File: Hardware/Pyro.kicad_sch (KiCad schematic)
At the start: 10 parts, among them J5 7788, J6 7788, Q1 BUK9M11-40EX, U12 TCMT1109

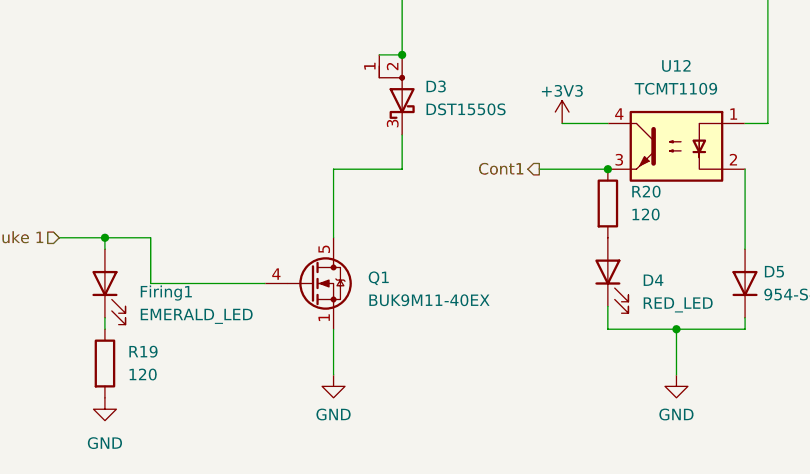
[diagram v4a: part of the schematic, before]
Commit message: GPIO broken out + post review 4
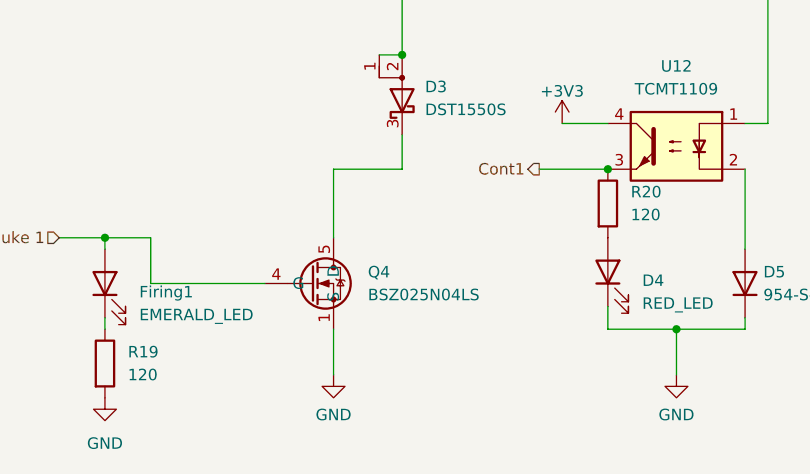
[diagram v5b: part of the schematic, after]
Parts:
- removed Q1: BUK9M11-40EX, Package_TO_SOT_SMD:LFPAK33, symbol Transistor_FET:BUK9M11-40EX
- added Q4: BSZ025N04LS, iclr:BSZ025N04LS, symbol iclr:BSZ025N04LS
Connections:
- net GND: now also Q4.1 (S), Q4.2 (S), Q4.3 (S), Q4.A1 (S)
- net Nuke 1: now also Q4.4 (G)
- net at D3.3 (K): now also Q4.5 (D), Q4.6 (D), Q4.7 (D), Q4.8 (D), Q4.A5 (D)
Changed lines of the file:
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@@
+	)
+	(symbol
+		(lib_id "iclr:BSZ025N04LS")
+		(at 114.3 95.25 0)
+		(unit 1)
+		(exclude_from_sim no)
+		(in_bom yes)
+		(on_board yes)
+		(dnp no)
+		(fields_autoplaced yes)
+		(property "Reference" "Q4"
+			(at 119.38 93.9799 0)
+			(effects
+				(font
+					(size 1.27 1.27)
+				)
+				(justify left)
+			)
+		)
+		(property "Value" "BSZ025N04LS"
+			(at 119.38 96.5199 0)
+			(effects
+				(font
+					(size 1.27 1.27)
+				)
+				(justify left)
+			)
+		)
+		(property "Footprint" "iclr:BSZ025N04LS"
+			(at 135.89 190.17 0)
+			(effects
+				(font
+					(size 1.27 1.27)
+				)
+				(justify left top)
+				(hide yes)
+			)
+		)
+		(property "Datasheet" "http://www.infineon.com/dgdl/DS_BSZ025N04LS_2_1.pdf?fileId=5546d46146d18cb40147204a34530283"
+			(at 135.89 290.17 0)
+			(effects
+				(font
+					(size 1.27 1.27)
+				)
+				(justify left top)
+				(hide yes)
+			)
+		)
+		(property "Description" "MOSFET MV POWER MOS MOSFET OptiMOS Power-MOSFET,40V"
+			(at 114.554 74.168 0)
+			(effects
+				(font
+					(size 1.27 1.27)
+				)
+				(hide yes)
+			)
+		)
+		(property "Height" "1.1"
+			(at 135.89 490.17 0)
+			(effects
+				(font
+					(size 1.27 1.27)
+				)
+				(justify left top)
+				(hide yes)
+			)
+		)
+		(property "Manufacturer_Name" "Infineon"
+			(at 135.89 590.17 0)
+			(effects
+				(font
+					(size 1.27 1.27)
+				)
+				(justify left top)
+				(hide yes)
+			)
+		)
+		(property "Manufacturer_Part_Number" "BSZ025N04LS"
+			(at 135.89 690.17 0)
+			(effects
+				(font
+					(size 1.27 1.27)
+				)
+				(justify left top)
+				(hide yes)
+			)
+		)
+		(property "Mouser Part Number" "726-BSZ025N04LS"
+			(at 135.89 790.17 0)
+			(effects
+				(font
+					(size 1.27 1.27)
+				)
+				(justify left top)
+				(hide yes)
+			)
+		)
+		(property "Mouser Price/Stock" "https://www.mouser.co.uk/ProductDetail/Infineon-Technologies/BSZ025N04LS?qs=glduVv6OWv6ppMJu86R39g%3D%3D"
+			(at 135.89 890.17 0)
+			(effects
+				(font
+					(size 1.27 1.27)
+				)
+				(justify left top)
+				(hide yes)
+			)
+		)
+		(property "Arrow Part Number" ""
+			(at 135.89 990.17 0)
+			(effects
+				(font
+					(size 1.27 1.27)
+				)
+				(justify left top)
+				(hide yes)
+			)
+		)
+		(property "Arrow Price/Stock" ""
+			(at 135.89 1090.17 0)
+			(effects
+				(font
+					(size 1.27 1.27)
+				)
+				(justify left top)
+				(hide yes)
+			)
+		)
+		(pin "6"
+		)
+		(pin "1"
+		)
+		(pin "A1"
+		)
+		(pin "A5"
+		)
+		(pin "7"
+		)
+		(pin "4"
+		)
+		(pin "5"
+		)
+		(pin "8"
+		)
+		(pin "2"
+		)
+		(pin "3"
+		)
+		(instances
+			(project "Main board"
+				(path "/7db990e4-92e1-4f99-b4d2-435bbec1ba83/2f4d1188-68cf-4851-a56c-97d43238a03a"
+					(reference "Q4")
+					(unit 1)
+				)
+			)
+		)
 	)
 	(symbol
@@
 					(unit 1)
 				)
-			)
-		)
-	)
-	(symbol
-		(lib_id "Transistor_FET:BUK9M11-40EX")
-		(at 113.03 95.25 0)
-		(unit 1)
-		(exclude_from_sim no)
-		(in_bom yes)
-		(on_board yes)
-		(dnp no)
-		(fields_autoplaced yes)
-		(property "Reference" "Q1"
-			(at 119.38 94.615 0)
-			(effects
-				(font
-					(size 1.27 1.27)
-				)
-				(justify left)
-			)
-		)
-		(property "Value" "BUK9M11-40EX"
-			(at 119.38 97.155 0)
-			(effects
-				(font
-					(size 1.27 1.27)
-				)
-				(justify left)
-			)
-		)
-		(property "Footprint" "Package_TO_SOT_SMD:LFPAK33"
-			(at 118.11 97.155 0)
-			(effects
-				(font
-					(size 1.27 1.27)
-					(italic yes)
-				)
-				(justify left)
-				(hide yes)
-			)
-		)
-		(property "Datasheet" "https://assets.nexperia.com/documents/data-sheet/BUK9M11-40E.pdf"
-			(at 113.03 95.25 90)
-			(effects
-				(font
-					(size 1.27 1.27)
-				)
-				(justify left)
-				(hide yes)
-			)
-		)
-		(property "Description" ""
-			(at 113.03 95.25 0)
-			(effects
-				(font
-					(size 1.27 1.27)
-				)
-				(hide yes)
-			)
-		)
-		(pin "1"
-		)
-		(pin "2"
-		)
-		(pin "3"
-		)
-		(pin "4"
-		)
-		(pin "5"
-		)
-		(instances
-			(project "Main board"
-				(path "/7db990e4-92e1-4f99-b4d2-435bbec1ba83/2f4d1188-68cf-4851-a56c-97d43238a03a"
-					(reference "Q1")
-					(unit 1)
-				)

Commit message: Mega commit
Post review changes
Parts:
- added R39: 10k, Resistor_SMD:R_0402_1005Metric, symbol Device:R_Small
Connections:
- net GND: now also R39.2
- net Nuke 1: now also R39.1
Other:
- moved on the sheet: Firing1, R19
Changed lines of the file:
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@@
+	)
+	(junction
+		(at 78.74 95.25)
+		(diameter 0)
+		(color 0 0 0 0)
 	)
 	(junction
@@
 	)
 	(junction
-		(at 90.17 90.17)
+		(at 90.17 95.25)
 		(diameter 0)
 		(color 0 0 0 0)
@@
 	(wire
 		(pts
-			(xy 90.17 99.06) (xy 90.17 100.33)
-		)
-		(stroke
-			(width 0)
-			(type default)
-		)
-	)
-	(wire
-		(pts
-			(xy 95.25 95.25) (xy 107.95 95.25)
+			(xy 78.74 95.25) (xy 90.17 95.25)
+		)
+		(stroke
+			(width 0)
+			(type default)
+		)
+	)
+	(wire
+		(pts
+			(xy 90.17 104.14) (xy 90.17 105.41)
 		)
 		(stroke
@@
 	(wire
 		(pts
-			(xy 95.25 90.17) (xy 95.25 95.25)
+			(xy 78.74 95.25) (xy 78.74 97.79)
 		)
 		(stroke
@@
 	(wire
 		(pts
-			(xy 85.09 90.17) (xy 90.17 90.17)
+			(xy 68.58 95.25) (xy 78.74 95.25)
 		)
 		(stroke
@@
 	(wire
 		(pts
-			(xy 90.17 90.17) (xy 95.25 90.17)
+			(xy 90.17 95.25) (xy 107.95 95.25)
+		)
+		(stroke
+			(width 0)
+			(type default)
+		)
+	)
+	(wire
+		(pts
+			(xy 78.74 102.87) (xy 78.74 113.03)
 		)
 		(stroke
@@
 	(wire
 		(pts
-			(xy 90.17 90.17) (xy 90.17 91.44)
+			(xy 90.17 95.25) (xy 90.17 96.52)
 		)
 		(stroke
@@
 	(hierarchical_label "Nuke 1"
 		(shape input)
-		(at 85.09 90.17 180)
+		(at 68.58 95.25 180)
 		(effects
 			(font
@@
 	)
 	(symbol
+		(lib_id "Device:R_Small")
+		(at 78.74 100.33 0)
+		(unit 1)
+		(exclude_from_sim no)
+		(in_bom yes)
+		(on_board yes)
+		(dnp no)
+		(property "Reference" "R39"
+			(at 75.438 99.568 0)
+			(effects
+				(font
+					(size 1.27 1.27)
+				)
+			)
+		)
+		(property "Value" "10k"
+			(at 75.3364 101.346 0)
+			(effects
+				(font
+					(size 1.27 1.27)
+				)
+			)
+		)
+		(property "Footprint" "Resistor_SMD:R_0402_1005Metric"
+			(at 78.74 100.33 0)
+			(effects
+				(font
+					(size 1.27 1.27)
+				)
+				(hide yes)
+			)
+		)
+		(property "Datasheet" "~"
+			(at 78.74 100.33 0)
+			(effects
+				(font
+					(size 1.27 1.27)
+				)
+				(hide yes)
+			)
+		)
+		(property "Description" ""
+			(at 78.74 100.33 0)
+			(effects
+				(font
+					(size 1.27 1.27)
+				)
+				(hide yes)
+			)
+		)
+		(pin "1"
+		)
+		(pin "2"
+		)
+		(instances
+			(project "Main board"
+				(path "/7db990e4-92e1-4f99-b4d2-435bbec1ba83/2f4d1188-68cf-4851-a56c-97d43238a03a"
+					(reference "R39")
+					(unit 1)
+				)
+			)
+		)
+	)
+	(symbol
 		(lib_id "power:GND")
-		(at 90.17 107.95 0)
+		(at 90.17 113.03 0)
 		(unit 1)
 		(exclude_from_sim no)
@@
 		(dnp no)
 		(property "Reference" "#PWR016"
-			(at 90.17 114.3 0)
+			(at 90.17 119.38 0)
 			(effects
 				(font
@@
 		)
 		(property "Value" "GND"
+			(at 90.17 118.11 0)
+			(effects
+				(font
+					(size 1.27 1.27)
+				)
+			)
+		)
+		(property "Footprint" ""
 			(at 90.17 113.03 0)
 			(effects
@@
 					(size 1.27 1.27)
 				)
-			)
-		)
-		(property "Footprint" ""
-			(at 90.17 107.95 0)
-			(effects
-				(font
-					(size 1.27 1.27)
-				)
 				(hide yes)
 			)
 		)
 		(property "Datasheet" ""
-			(at 90.17 107.95 0)
+			(at 90.17 113.03 0)
 			(effects
 				(font
@@
 		)
 		(property "Description" ""
-			(at 90.17 107.95 0)
+			(at 90.17 113.03 0)
 			(effects
 				(font
@@
 	)
 	(symbol
+		(lib_id "power:GND")
+		(at 78.74 113.03 0)
+		(unit 1)
+		(exclude_from_sim no)
+		(in_bom yes)
+		(on_board yes)
+		(dnp no)
+		(property "Reference" "#PWR073"
+			(at 78.74 119.38 0)
+			(effects
+				(font
+					(size 1.27 1.27)
+				)
+				(hide yes)
+			)
+		)
+		(property "Value" "GND"
+			(at 78.74 118.11 0)
+			(effects
+				(font
+					(size 1.27 1.27)
+				)
+			)
+		)
+		(property "Footprint" ""
+			(at 78.74 113.03 0)
+			(effects
+				(font
+					(size 1.27 1.27)
+				)
+				(hide yes)
+			)
+		)
+		(property "Datasheet" ""
+			(at 78.74 113.03 0)
+			(effects
+				(font
+					(size 1.27 1.27)
+				)
+				(hide yes)
+			)
+		)
+		(property "Description" ""
+			(at 78.74 113.03 0)
+			(effects
+				(font
+					(size 1.27 1.27)
+				)
+				(hide yes)
+			)
+		)
+		(pin "1"
+		)
+		(instances
+			(project "Main board"
+				(path "/7db990e4-92e1-4f99-b4d2-435bbec1ba83/2f4d1188-68cf-4851-a56c-97d43238a03a"
+					(reference "#PWR073")
+					(unit 1)
+				)
+			)
+		)
+	)
+	(symbol
 		(lib_id "Device:R")
-		(at 90.17 104.14 0)
+		(at 90.17 109.22 0)
 		(unit 1)
 		(exclude_from_sim no)
@@
 		(fields_autoplaced yes)
 		(property "Reference" "R19"
-			(at 92.71 102.8699 0)
+			(at 92.71 107.9499 0)
 			(effects
 				(font
@@
 		)
 		(property "Value" "120"
-			(at 92.71 105.4099 0)
+			(at 92.71 110.4899 0)
 			(effects
 				(font
@@
 		)
 		(property "Footprint" "Resistor_SMD:R_0402_1005Metric"
-			(at 88.392 104.14 90)
+			(at 88.392 109.22 90)
 			(effects
 				(font
@@
 		)
 		(property "Datasheet" "~"
-			(at 90.17 104.14 0)
+			(at 90.17 109.22 0)
 			(effects
 				(font
@@
 		)
 		(property "Description" ""
-			(at 90.17 104.14 0)
+			(at 90.17 109.22 0)
 			(effects
 				(font
@@
 	(symbol
 		(lib_id "Device:LED")
-		(at 90.17 95.25 90)
+		(at 90.17 100.33 90)
 		(unit 1)
 		(exclude_from_sim no)
@@
 		(fields_autoplaced yes)
 		(property "Reference" "Firing1"
-			(at 93.98 96.2025 90)
+			(at 93.98 101.2825 90)
 			(effects
 				(font
@@
 		)
 		(property "Value" "EMERALD_LED"
-			(at 93.98 98.7425 90)
+			(at 93.98 103.8225 90)
 			(effects
 				(font
@@
 		)
 		(property "Footprint" "LED_SMD:LED_0402_1005Metric"
-			(at 90.17 95.25 0)
+			(at 90.17 100.33 0)
 			(effects
 				(font
@@
 		)
 		(property "Datasheet" "~"
-			(at 90.17 95.25 0)
+			(at 90.17 100.33 0)
 			(effects
 				(font
@@
 		)
 		(property "Description" ""
-			(at 90.17 95.25 0)
-			(effects
-				(font
+			(at 90.17 100.33 0)
+			(effects
+				(font

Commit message: V2 changes, PCB finished
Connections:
- net PYRO-ve: now reaches D3.1 (A), D3.2 (A), J6.1, J6.2, J6.3, J6.4, U12.1
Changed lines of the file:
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@@
+		)
+	)
+	(label "PYRO-ve"
+		(at 133.35 59.69 0)
+		(effects
+			(font
+				(size 1.27 1.27)
+			)
+			(justify left bottom)
 		)
 	)

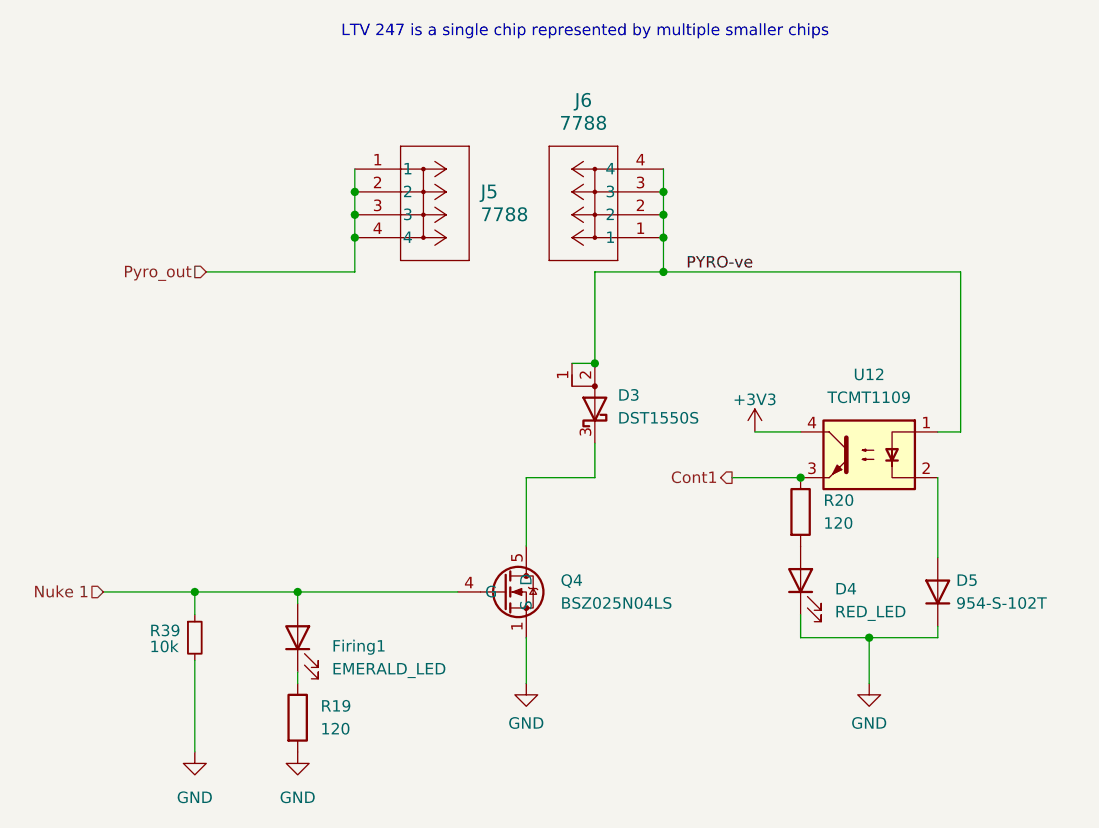
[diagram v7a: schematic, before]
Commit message: More V2 changes
Mainly changed to use Ω symbol for resistors. Fixed the CDC pin for the buck boost
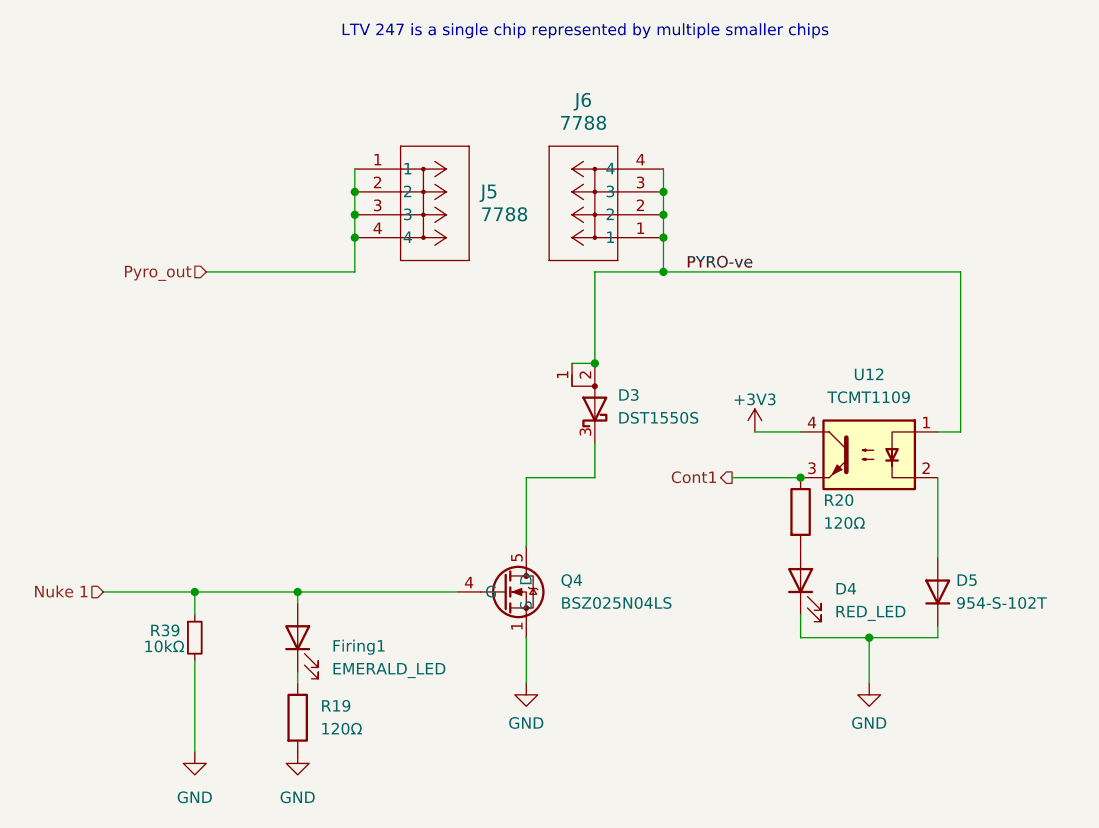
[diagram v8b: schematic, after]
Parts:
- R19, R20: value 120 -> 120Ω
- R39: value 10k -> 10kΩ
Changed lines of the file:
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@@
 			)
 		)
-		(property "Value" "10k"
+		(property "Value" "10kΩ"
 			(at 75.3364 101.346 0)
 			(effects
@@
 			)
 		)
-		(property "Value" "120"
+		(property "Value" "120Ω"
 			(at 92.71 110.4899 0)
 			(effects
@@
 			)
 		)
-		(property "Value" "120"
+		(property "Value" "120Ω"
 			(at 148.59 87.6299 0)
 			(effects
